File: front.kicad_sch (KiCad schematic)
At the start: 17 parts, among them SW1 SW_Push, SW2 SW_Push, SW3 SW_Push, SW4 SW_Push, SW5 SW_Push, U5 SCD40_Breakout, U6 AHT20

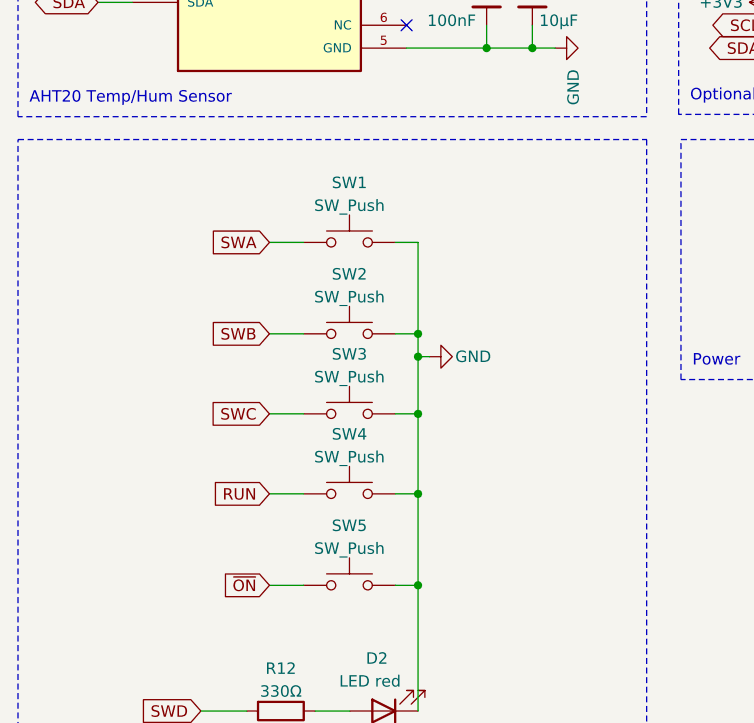
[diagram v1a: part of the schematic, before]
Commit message: switch to user:SW_PUSH
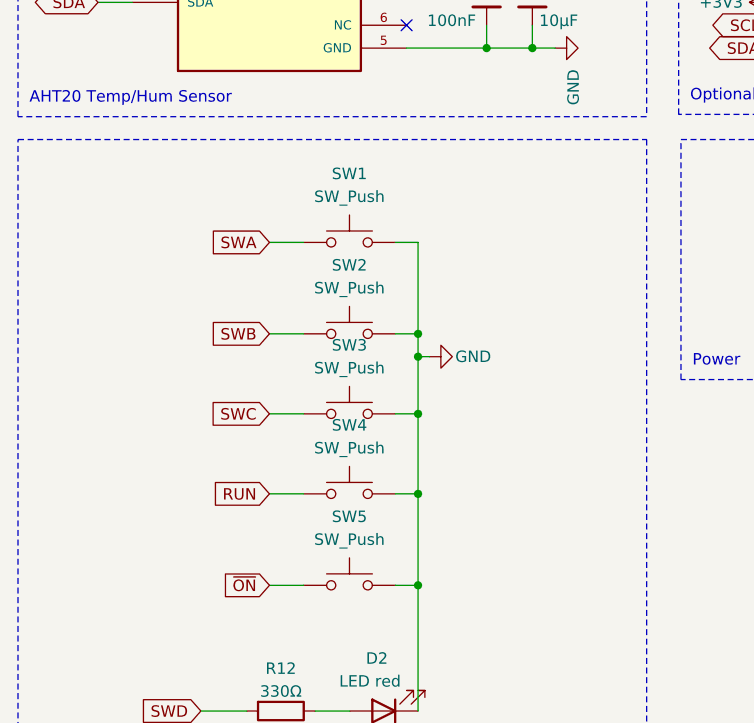
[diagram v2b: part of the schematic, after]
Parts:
- SW1, SW2, SW3, SW4, SW5: footprint Button_Switch_SMD:SW_SPST_B3S-1000 -> user:SW_SPST_B3S-1000; symbol Switch:SW_Push -> user:SW_Push
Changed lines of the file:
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@@
     )
   )
-  (symbol (lib_id "Switch:SW_Push") (at 54.61 83.82 0) (unit 1)
-    (in_bom yes) (on_board yes) (dnp no) (fields_autoplaced)
-    (property "Reference" "SW3" (at 54.61 77.1992 0)
-      (effects (font (size 1.27 1.27)))
-    )
-    (property "Value" "SW_Push" (at 54.61 79.7361 0)
-      (effects (font (size 1.27 1.27)))
-    )
-    (property "Footprint" "Button_Switch_SMD:SW_SPST_B3S-1000" (at 54.61 78.74 0)
+  (symbol (lib_id "user:SW_Push") (at 54.61 83.82 0) (unit 1)
+    (in_bom yes) (on_board yes) (dnp no) (fields_autoplaced)
+    (property "Reference" "SW3" (at 54.61 76.2 0)
+      (effects (font (size 1.27 1.27)))
+    )
+    (property "Value" "SW_Push" (at 54.61 78.74 0)
+      (effects (font (size 1.27 1.27)))
+    )
+    (property "Footprint" "user:SW_SPST_B3S-1000" (at 54.61 88.9 0)
       (effects (font (size 1.27 1.27)) hide)
     )
@@
     )
   )
-  (symbol (lib_id "Switch:SW_Push") (at 54.61 64.77 0) (unit 1)
-    (in_bom yes) (on_board yes) (dnp no) (fields_autoplaced)
-    (property "Reference" "SW1" (at 54.61 58.1492 0)
-      (effects (font (size 1.27 1.27)))
-    )
-    (property "Value" "SW_Push" (at 54.61 60.6861 0)
-      (effects (font (size 1.27 1.27)))
-    )
-    (property "Footprint" "Button_Switch_SMD:SW_SPST_B3S-1000" (at 54.61 59.69 0)
+  (symbol (lib_id "user:SW_Push") (at 54.61 64.77 0) (unit 1)
+    (in_bom yes) (on_board yes) (dnp no) (fields_autoplaced)
+    (property "Reference" "SW1" (at 54.61 57.15 0)
+      (effects (font (size 1.27 1.27)))
+    )
+    (property "Value" "SW_Push" (at 54.61 59.69 0)
+      (effects (font (size 1.27 1.27)))
+    )
+    (property "Footprint" "user:SW_SPST_B3S-1000" (at 54.61 69.85 0)
       (effects (font (size 1.27 1.27)) hide)
     )
@@
     )
   )
-  (symbol (lib_id "Switch:SW_Push") (at 54.61 92.71 0) (unit 1)
-    (in_bom yes) (on_board yes) (dnp no) (fields_autoplaced)
-    (property "Reference" "SW4" (at 54.61 86.0892 0)
-      (effects (font (size 1.27 1.27)))
-    )
-    (property "Value" "SW_Push" (at 54.61 88.6261 0)
-      (effects (font (size 1.27 1.27)))
-    )
-    (property "Footprint" "Button_Switch_SMD:SW_SPST_B3S-1000" (at 54.61 87.63 0)
+  (symbol (lib_id "user:SW_Push") (at 54.61 92.71 0) (unit 1)
+    (in_bom yes) (on_board yes) (dnp no) (fields_autoplaced)
+    (property "Reference" "SW4" (at 54.61 85.09 0)
+      (effects (font (size 1.27 1.27)))
+    )
+    (property "Value" "SW_Push" (at 54.61 87.63 0)
+      (effects (font (size 1.27 1.27)))
+    )
+    (property "Footprint" "user:SW_SPST_B3S-1000" (at 54.61 97.79 0)
       (effects (font (size 1.27 1.27)) hide)
     )
@@
     )
   )
-  (symbol (lib_id "Switch:SW_Push") (at 54.61 74.93 0) (unit 1)
-    (in_bom yes) (on_board yes) (dnp no) (fields_autoplaced)
-    (property "Reference" "SW2" (at 54.61 68.3092 0)
-      (effects (font (size 1.27 1.27)))
-    )
-    (property "Value" "SW_Push" (at 54.61 70.8461 0)
-      (effects (font (size 1.27 1.27)))
-    )
-    (property "Footprint" "Button_Switch_SMD:SW_SPST_B3S-1000" (at 54.61 69.85 0)
+  (symbol (lib_id "user:SW_Push") (at 54.61 74.93 0) (unit 1)
+    (in_bom yes) (on_board yes) (dnp no) (fields_autoplaced)
+    (property "Reference" "SW2" (at 54.61 67.31 0)
+      (effects (font (size 1.27 1.27)))
+    )
+    (property "Value" "SW_Push" (at 54.61 69.85 0)
+      (effects (font (size 1.27 1.27)))
+    )
+    (property "Footprint" "user:SW_SPST_B3S-1000" (at 54.61 80.01 0)
       (effects (font (size 1.27 1.27)) hide)
     )
@@
     )
   )
-  (symbol (lib_id "Switch:SW_Push") (at 54.61 102.87 0) (unit 1)
-    (in_bom yes) (on_board yes) (dnp no) (fields_autoplaced)
-    (property "Reference" "SW5" (at 54.61 96.2492 0)
-      (effects (font (size 1.27 1.27)))
-    )
-    (property "Value" "SW_Push" (at 54.61 98.7861 0)
-      (effects (font (size 1.27 1.27)))
-    )
-    (property "Footprint" "Button_Switch_SMD:SW_SPST_B3S-1000" (at 54.61 97.79 0)
-      (effects (font (size 1.27 1.27)) hide)
-    )
+  (symbol (lib_id "user:SW_Push") (at 54.61 102.87 0) (unit 1)
+    (in_bom yes) (on_board yes) (dnp no) (fields_autoplaced)
+    (property "Reference" "SW5" (at 54.61 95.25 0)
+      (effects (font (size 1.27 1.27)))
+    )
+    (property "Value" "SW_Push" (at 54.61 97.79 0)
+      (effects (font (size 1.27 1.27)))
+    )
+    (property "Footprint" "user:SW_SPST_B3S-1000" (at 54.61 107.95 0)
+      (effects (font (size 1.27 1.27)) hide)
+    )
